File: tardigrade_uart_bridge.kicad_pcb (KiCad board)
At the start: 2 copper layers, 50.8 x 50.8 mm, 19 parts, among them J1 Conn_01x06_Socket, J5 Conn_01x05_Socket, J6 S4B-PH-K-S, J7 S8B-PH-K-S, U1 ATmega328P-A, U2 AZ1117H-3.3TRE1, Y1 Crystal

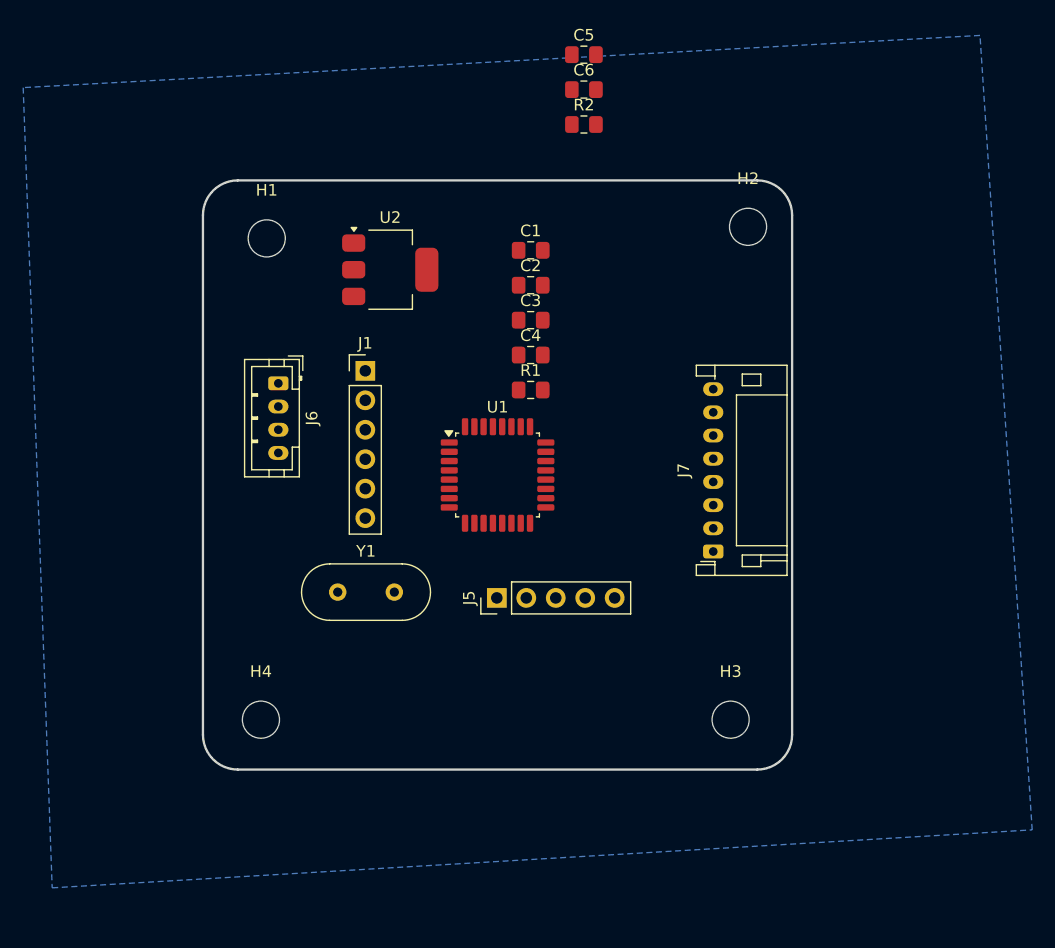
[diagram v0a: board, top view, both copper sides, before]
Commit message: added pwm outputs, power connectors, etc.
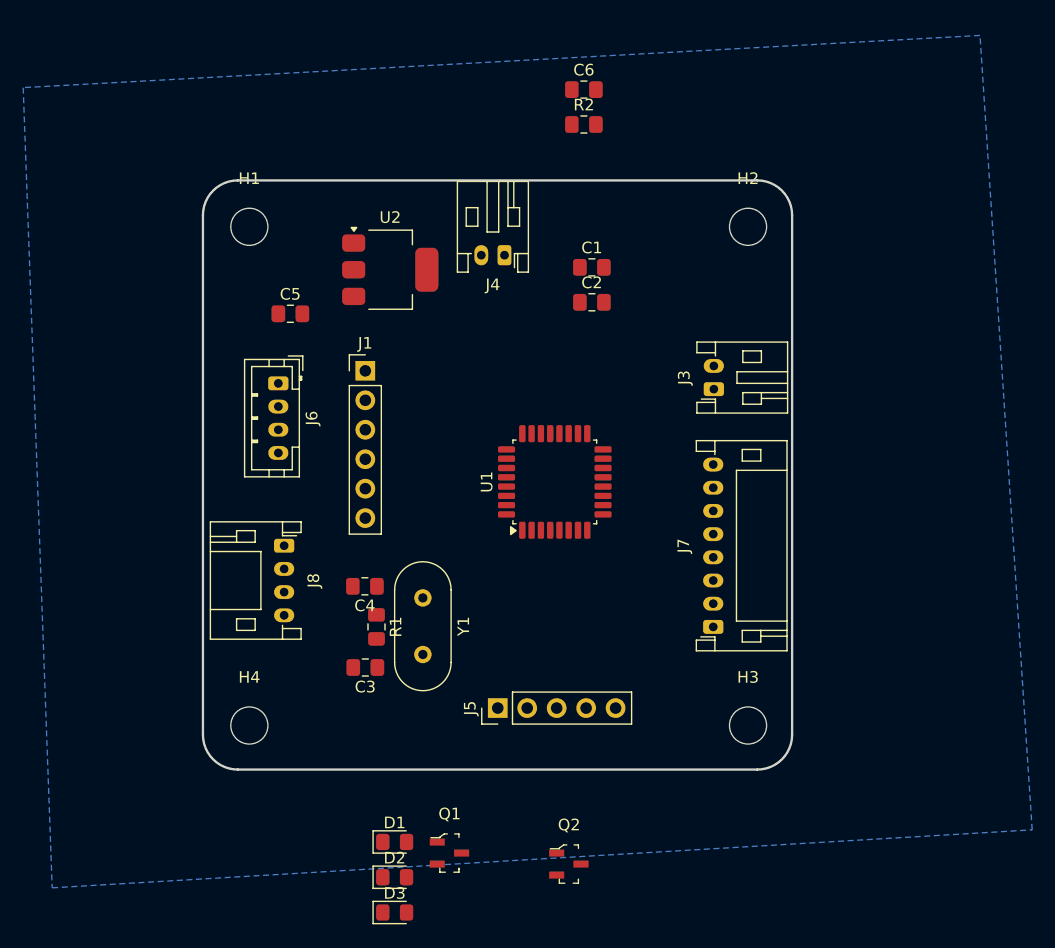
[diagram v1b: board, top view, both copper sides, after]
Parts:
- added D1: LED_TX, LED_SMD:LED_0805_2012Metric_Pad1.15x1.40mm_HandSolder, F.Cu at (79.0, 104.0)
- added D2: LED_TX, LED_SMD:LED_0805_2012Metric_Pad1.15x1.40mm_HandSolder, F.Cu at (79.0, 107.1)
- added D3: LED_PWR, LED_SMD:LED_0805_2012Metric_Pad1.15x1.40mm_HandSolder, F.Cu at (79.0, 110.1)
- added J3: S2B-PH-K-S, Connector_JST:JST_PH_S2B-PH-K_1x02_P2.00mm_Horizontal, F.Cu at (106.5, 65.0)
- added J4: S2B-PH-K-S, Connector_JST:JST_PH_S2B-PH-K_1x02_P2.00mm_Horizontal, F.Cu at (88.5, 53.5)
- added J8: S4B-PH-K-S, Connector_JST:JST_PH_S4B-PH-K_1x04_P2.00mm_Horizontal, F.Cu at (69.5, 78.5)
- added Q1: MMBT2222A-TP, digikey-footprints:SOT-23-3, F.Cu at (83.8, 105.0)
- added Q2: MMBT2222A-TP, digikey-footprints:SOT-23-3, F.Cu at (94.0, 106.0)
- moved C5 33.8 mm to (70.0, 58.5)
- moved C3 33.2 mm to (76.5, 89.0), turned to 180 degrees
- moved C4 24.5 mm to (76.5, 82.0), turned to 180 degrees
- moved R1 24.4 mm to (77.5, 85.5), turned to -90 degrees
- moved J5 9.50 mm to (87.9, 92.5)
- moved Y1 7.36 mm to (81.5, 83.0), turned to -90 degrees
- moved J7 6.50 mm to (106.5, 85.5)
- moved C1 5.48 mm to (96.0, 54.5)
- moved C2 5.48 mm to (96.0, 57.5)
- moved U1 4.97 mm to (92.8, 73.0), turned to 90 degrees
- moved H1 1.80 mm to (66.5, 51.0)
- moved H3 1.58 mm to (109.5, 94.0)
- moved H4 1.12 mm to (66.5, 94.0)
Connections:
- C6 pad 1: 3.3V -> Net-(U2-VO)
- J7 pad 6: /PWM4 -> /ICSP_MISO
- U1 pad 1: unconnected-(U1-PD3-Pad1) -> /PWM5
- U1 pad 10: unconnected-(U1-PD6-Pad10) -> /PWM0
- U1 pad 13: unconnected-(U1-PB1-Pad13) -> /PWM2
- U1 pad 14: unconnected-(U1-PB2-Pad14) -> /PWM3
- U1 pad 15: unconnected-(U1-PB3-Pad15) -> /ICSP_MISO
- U1 pad 16: unconnected-(U1-PB4-Pad16) -> /ICSP_MOSI
- U1 pad 17: unconnected-(U1-PB5-Pad17) -> /ICSP_SCK
- U1 pad 27: unconnected-(U1-PC4-Pad27) -> /I2C_SDA
- U1 pad 28: unconnected-(U1-PC5-Pad28) -> /I2C_SCL
- U1 pad 30: unconnected-(U1-PD0-Pad30) -> /UART_HOST_TX
- U1 pad 31: unconnected-(U1-PD1-Pad31) -> /UART_HOST_RX
- U1 pad 9: unconnected-(U1-PD5-Pad9) -> /PWM1
- U2 pad 2: 3.3V -> Net-(U2-VO)
